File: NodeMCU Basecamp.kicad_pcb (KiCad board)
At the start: 2 copper layers, 63.5 x 50.8 mm, 47 parts, among them Q1 BSS138, Q10 BSS138, Q11 BSS138, Q12 BSS138, Q13 BSS138, Q2 BSS138, Q3 BSS138, Q4 BSS138, Q5 BSS138, Q6 BSS138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

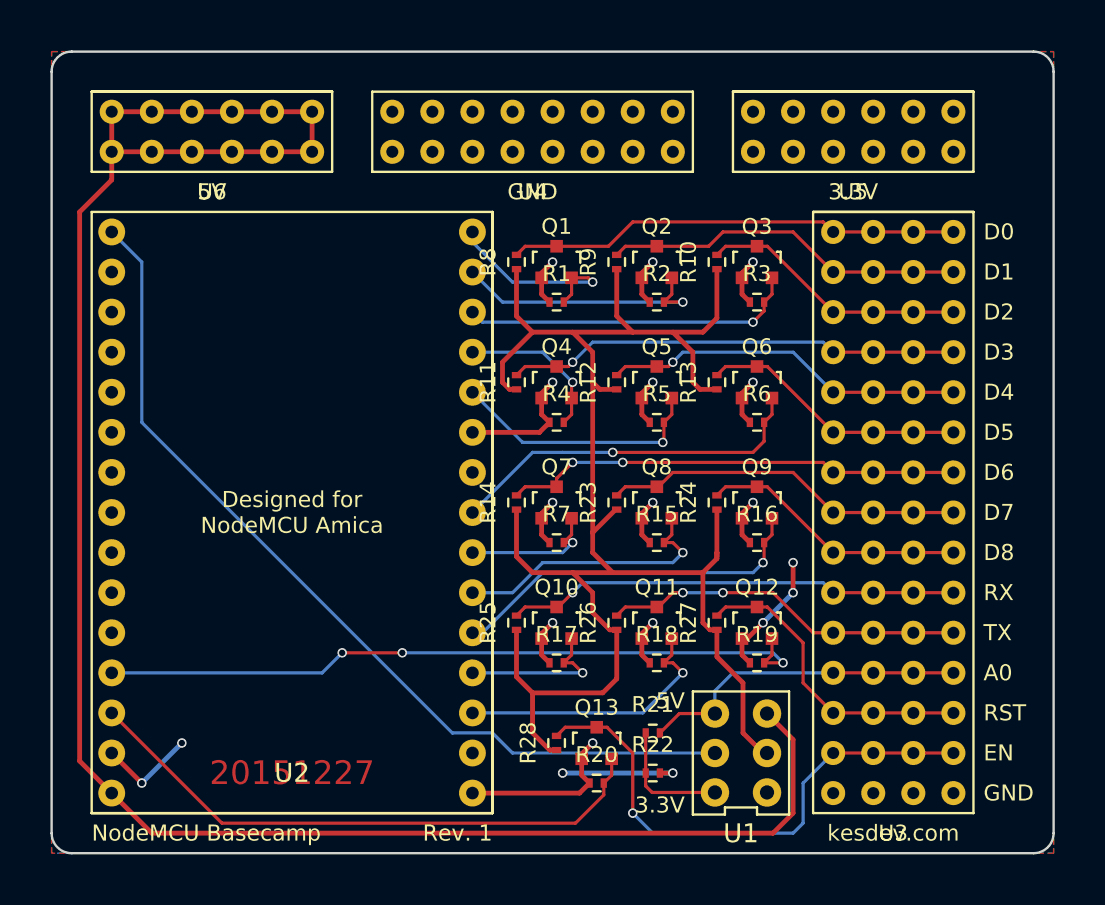
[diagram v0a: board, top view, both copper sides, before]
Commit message: pcb: improvements to text, fills, islands, drill sizes
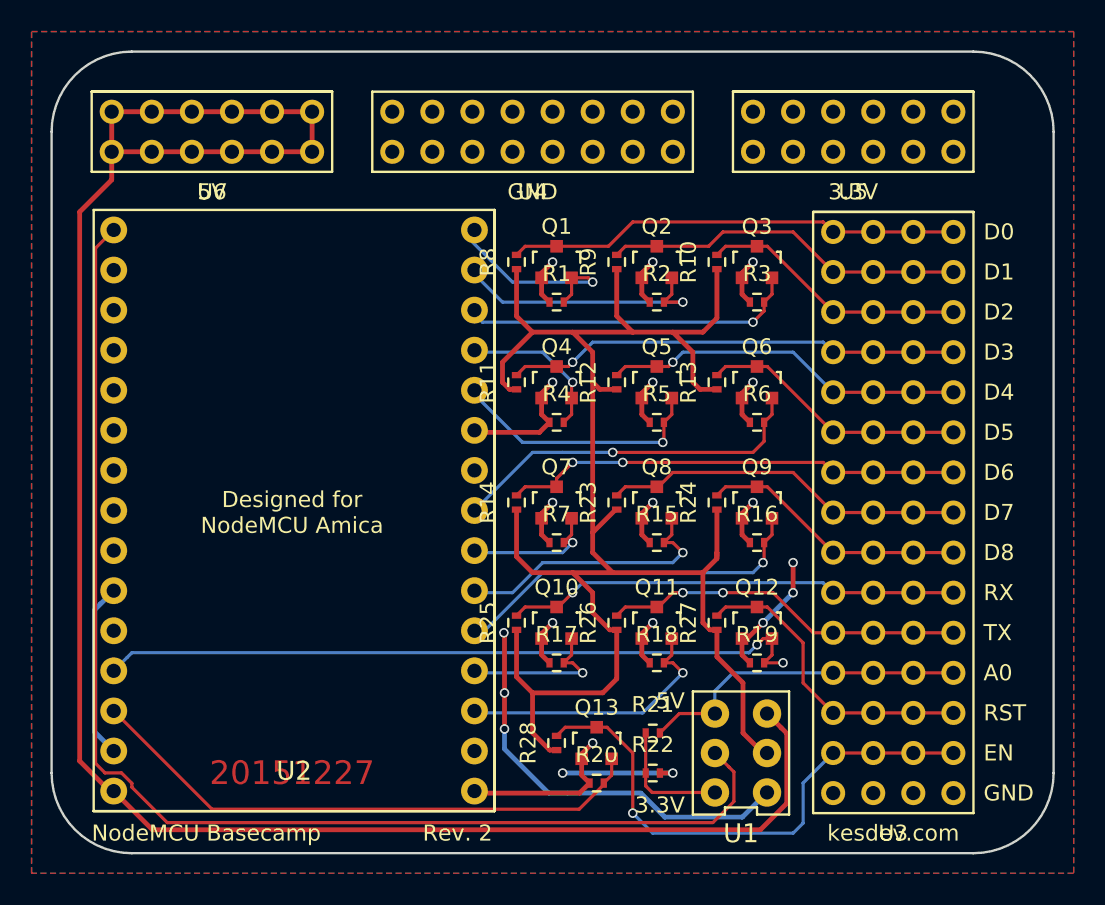
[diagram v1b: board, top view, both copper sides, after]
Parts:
- turned U2 to 0 degrees
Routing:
- net 3V3: track 57.5 -> 84.0 mm, vias 15 -> 18
- net A0_LV: track 57.9 -> 80.6 mm
- net Earth: track 14.1 -> 19.0 mm, vias 4 -> 2
- net RST_LV: track 37.3 -> 36.1 mm
- net 5V: track 124.6 -> 123.4 mm
- net EN_LV: track 46.3 -> 45.5 mm, vias 3 -> 2
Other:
- outline, holes or cut-outs redrawn
- board text added: "Rev. 2"
- board text removed: "Rev. 1"
